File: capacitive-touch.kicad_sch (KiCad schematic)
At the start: 12 parts, among them J2 Conn_01x04_MountingPin, J4 Conn_01x32, U8 CY8C20666A-24LQXI

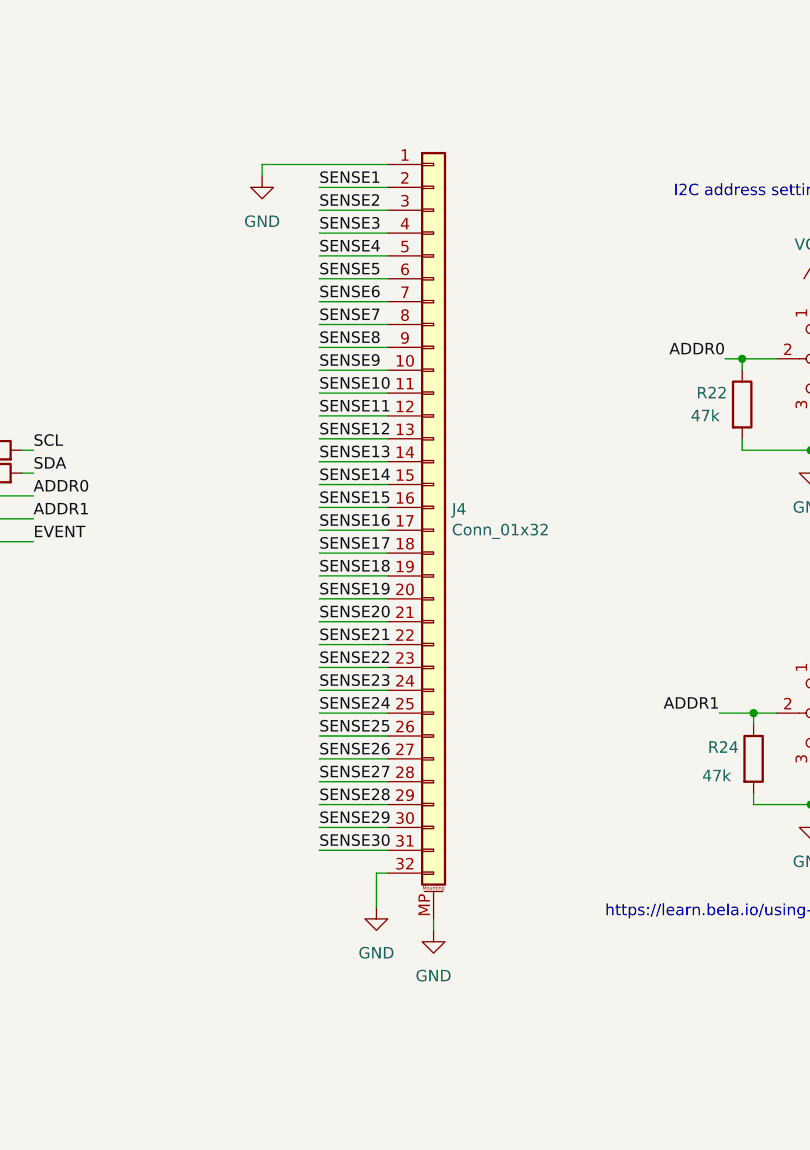
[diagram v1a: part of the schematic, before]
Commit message: new FET
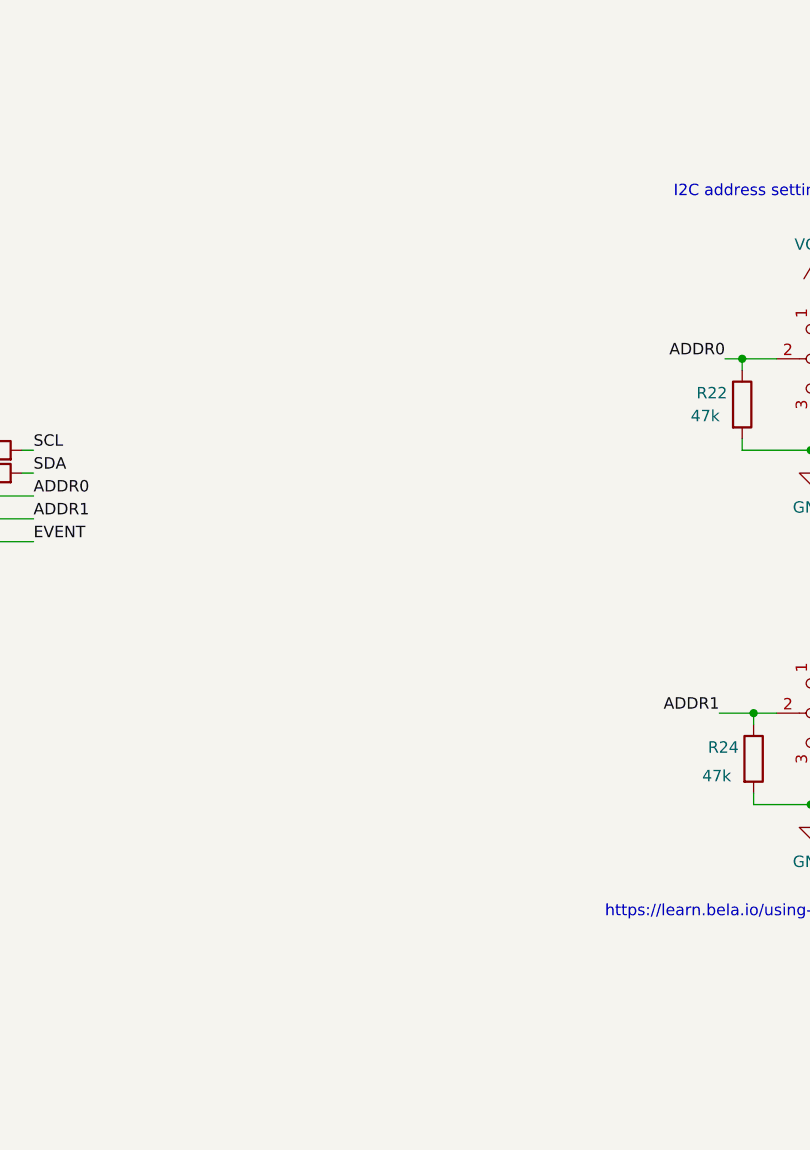
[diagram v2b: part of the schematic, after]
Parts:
- removed J4: Conn_01x32, Connector_FFC-FPC:Hirose_FH12-32S-0.5SH_1x32-1MP_P0.50mm_Horizontal, symbol Connector_Generic_MountingPin:Conn_01x32_MountingPin

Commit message: touch pcb
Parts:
- added CS1: TRILL_BAR-26_CapSense, TRILL:TRILL_BAR_CapSense, symbol Bela:TRILL_BAR-26_CapSense
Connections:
- net SENSE27 is gone; now on net SENSE23: U8.11 (P3[1])
- net SENSE28 is gone; now on net SENSE24: U8.12 ((SCL)P1[7])
- net SENSE29 is gone; now on net SENSE25: U8.13 ((SDA)P1[5])
- net SENSE30 is gone; now on net SENSE26: U8.16 (P1[3])
- net SENSE1: now also CS1.1
- net SENSE10: now also CS1.10
- net SENSE11: now also CS1.11
- net SENSE12: now also CS1.12
- net SENSE13: now also CS1.13
- net SENSE14: now also CS1.14
- net SENSE15: now also CS1.15
- net SENSE16: now also CS1.16
- net SENSE17: now also CS1.17
- net SENSE18: now also U8.6 (P4[3]), CS1.18; no longer U8.2 (P2[7])
- net SENSE19: now also U8.7 (P4[1]), CS1.19; no longer U8.3 (P2[5])
- net SENSE2: now also CS1.2
- net SENSE20: now also U8.8 (P3[7]), CS1.20; no longer U8.4 (P2[3])
- net SENSE21: now also U8.9 (P3[5]), CS1.21; no longer U8.5 (P2[1])
- net SENSE22: now also U8.10 (P3[3]), CS1.22; no longer U8.6 (P4[3])
- net SENSE23: now also CS1.23; no longer U8.7 (P4[1])
- net SENSE24: now also CS1.24; no longer U8.8 (P3[7])
- net SENSE25: now also CS1.25; no longer U8.9 (P3[5])
- net SENSE26: now also CS1.26; no longer U8.10 (P3[3])
- net SENSE3: now also CS1.3
- net SENSE4: now also CS1.4
- net SENSE5: now also CS1.5
- net SENSE6: now also CS1.6
- net SENSE7: now also CS1.7
- net SENSE8: now also CS1.8
- net SENSE9: now also CS1.9
- no-connect marks 0 -> 4

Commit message: updated components
New ganfet selected and further work developing the rp2040 microcontroller circuit
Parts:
- removed J2: Conn_01x04_MountingPin, TRILL:qwiic_horizontal_SMD, symbol Connector_Generic_MountingPin:Conn_01x04_MountingPin
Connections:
- net VCC: now also JP4.1 (A)
- net EVENT: no longer names the net of U8.25 (P1[6])
- net GND renamed GND1
- net XRES: no longer names the net of U8.26 (XRES)
- no-connect marks 4 -> 6
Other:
- note removed: "https://www.sparkfun.com/qwiic"
- note removed: "qwiic connector"

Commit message: finished board
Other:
- moved on the sheet: G5
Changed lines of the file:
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@@
 	(title_block
 		(title "Replacable LED COB Lamp")
-		(date "2025-03-24")
+		(date "2025-04-08")
 		(rev "0")
 		(company "WPI ECE2799 D25")
@@
 	(symbol
 		(lib_id "TRILL:OpenSourceHardware_Logo")
-		(at 83.185 182.245 0)
+		(at 254 137.16 0)
 		(unit 1)
 		(exclude_from_sim no)
@@
 		(dnp no)
 		(property "Reference" "G5"
-			(at 81.915 178.435 0)
+			(at 250.444 133.604 0)
 			(effects
 				(font
@@
 		)
 		(property "Value" "OpenSourceHardware_Logo"
-			(at 76.835 180.34 0)
+			(at 250.444 136.144 0)
 			(effects
 				(font
@@
 		)
 		(property "Footprint" "TRILL:OpenSourceHardware_Logo"
-			(at 83.185 182.245 0)
+			(at 254 137.16 0)
 			(effects
 				(font
@@
 		)
 		(property "Datasheet" ""
-			(at 83.185 182.245 0)
+			(at 254 137.16 0)
 			(effects
 				(font
@@
 		)
 		(property "Description" ""
-			(at 83.185 182.245 0)
-			(effects
-				(font
-					(size 1.27 1.27)
-				)
+			(at 254 137.16 0)
+			(effects
+				(font
+					(size 1.27 1.27)
+				)
+				(hide yes)
 			)
 		)
 		(property "Part Number" ""
-			(at 83.185 182.245 0)
-			(effects
-				(font
-					(size 1.27 1.27)
-				)
-			)
-		)
+			(at 254 137.16 0)
+			(effects
+				(font
+					(size 1.27 1.27)
+				)
+				(hide yes)
+			)
+		)

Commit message: production design files
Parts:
- added H3, H4, H5, H6: MountingHole, MountingHole:MountingHole_3.2mm_M3, symbol Mechanical:MountingHole
- U8: Part Number (none) -> 448-CY8C20646A-24LQXI-ND
